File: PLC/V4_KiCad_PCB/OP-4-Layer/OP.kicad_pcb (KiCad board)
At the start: 4 copper layers, 208 x 80 mm, 307 parts, among them J1 MSTBVA-2.5-10-5.08, J10 01x03_fem, J11 01x02_fem, J12 01x15_fem, J13 01x03_fem, J14 01x15_fem, J15 01x04_fem, J16 MSTBVA-2.5-10-5.08, J17 MSTBVA-2.5-10-5.08, J2 MSTBVA-2.5-10-5.08, J25 01x05_fem, J27 Lötauge, J28 GND_CAN opt an J33, J3 PFS 2x4, J33 opt. GND_XXX, J37 Lötauge, J4 01x08_fem, J40 Extention, J41 Lötauge, J42 Lötauge, J43 Flachstecker, J44 Lötauge, J45 Lötauge, J46 Lötauge, J47 Lötauge, J48 Lötauge, J5 01x04_fem, J51 Lötauge, J52 Lötauge, J6 DIN-5, J61 Lötauge, J62 Lötauge, J7 DIN-5, J8 02x02_fem, J9 Ub 0V PE, P1 1,0K lin, P2 1,0K lin, Q1 IRLML 2244, SW1 SW_DIP_x02, SW2 SW_DIP_x02, SW3 SW_DIP_x02, U1 LTV-844, U10 ADM2483xRW, U2 LTV-844, U3 LTV-844, U36 MCP3204, U39 ADuM1401xRW, U4 LTV-844, U40 ADM-803R, U42 LM4040 AIM3-2.5, U43 LM4040 AIM3-2.5, U47 ADM-809Z, U48 ADM-803L, U49 74AHC1G32, U5 MCP23S17, U50 NE555DRG4, U6 ISO1050, U7 Teensy4.0, U8 ISO1050, U9 25LC512

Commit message: Kaltstart Überarbeitung
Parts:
- removed R50: 10k, Resistors_SMD:R_1206
- removed U40: ADM-803R, TO_SOT_Packages_SMD:SOT-23
- added C99: 100n, Capacitors_SMD:C_1206, F.Cu at (243.6, 76.6)
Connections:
- net /5V_CPU renamed Net-(C50-Pad1)
- net /COLDSTART_3V3INT renamed /3V3EN_Q2_UP
- C24 pad 2: /3V3_INTERFACE -> /3V3_INT
- C4 pad 1: /3V3_INTERFACE -> /3V3_INT
- C7 pad 2: /3V3_INTERFACE -> /3V3_INT
- C8 pad 1: /3V3_INTERFACE -> /3V3_INT
- D41 pad 2: /3V3_INTERFACE -> /3V3_INT
- J25 pad 1: /3V3_INTERFACE -> /3V3_INT
- J51 pad 1: /3V3_INTERFACE -> /3V3_INT
- R118 pad 2: /3V3_INTERFACE -> /3V3_INT
- U10 pad 1: /3V3_INTERFACE -> /3V3_INT
- U39 pad 1: /3V3_INTERFACE -> /3V3_INT
- U47 pad 3: /3V3_INTERFACE -> /3V3_INT
- U6 pad 1: /3V3_INTERFACE -> /3V3_INT
- U8 pad 1: /3V3_INTERFACE -> /3V3_INT
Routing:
- net /3V3_INTERFACE: track 182.9 -> 0.00 mm, vias 9 -> 0
- net /3V3_INT: track 217.4 -> 399.4 mm, vias 7 -> 16
- net GNDD: track 764.6 -> 762.6 mm, vias 162 -> 164

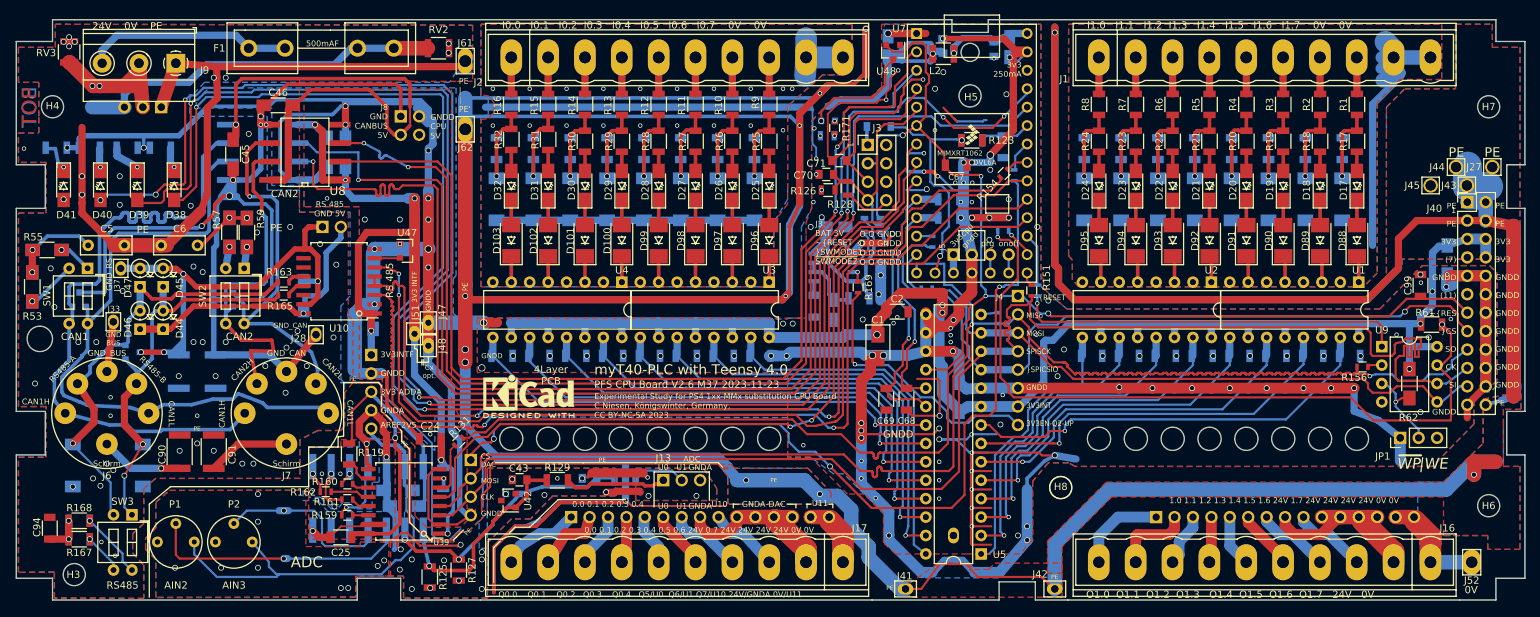
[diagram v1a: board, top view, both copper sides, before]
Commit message: Überarbeitung 4-Layer-Layout und Dokumentation
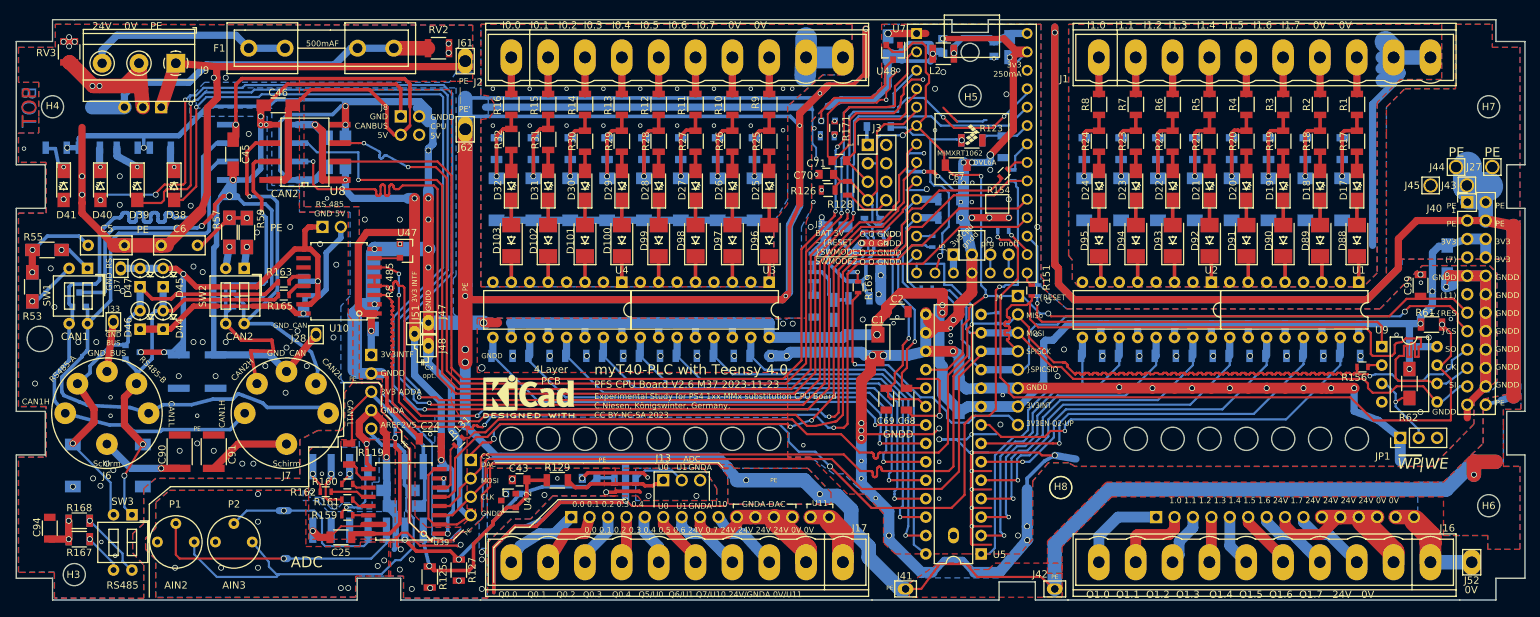
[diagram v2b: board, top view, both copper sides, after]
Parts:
- moved R155 0.13 mm to (187.5, 61.5)
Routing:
- net /3V3_INT: track 399.4 -> 421.1 mm
- net /GND_CAN_BUS: track 142.1 -> 151.8 mm
- net GNDA: track 67.8 -> 68.6 mm
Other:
- board text added: "In1"
- board text added: "In2"

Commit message: V2.6 R38 final PFS
M38 final Version for PFS variant
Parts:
- added R501: 10k, Resistors_SMD:R_1206, F.Cu at (245.4, 76.7)
- moved C99 0.51 mm to (243.1, 76.6)
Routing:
- net GNDD: track 762.6 -> 757.9 mm
- net /PE: track 1070.4 -> 1068.7 mm
- net /~EE_HOLD: vias 3 -> 2
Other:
- board text added: "PE PE 3V3 (7) (11) ~RES ~CS SO CK SI GNDD"
- board text added: "PFS CPU Board V2.6 M38 2024-01-17"
- board text removed: "PE PE 3V3 (7) GNDD (11) ~RES ~CS SO CK SI GNDD"
- board text removed: "PFS CPU Board V2.6 M37 2023-11-23"

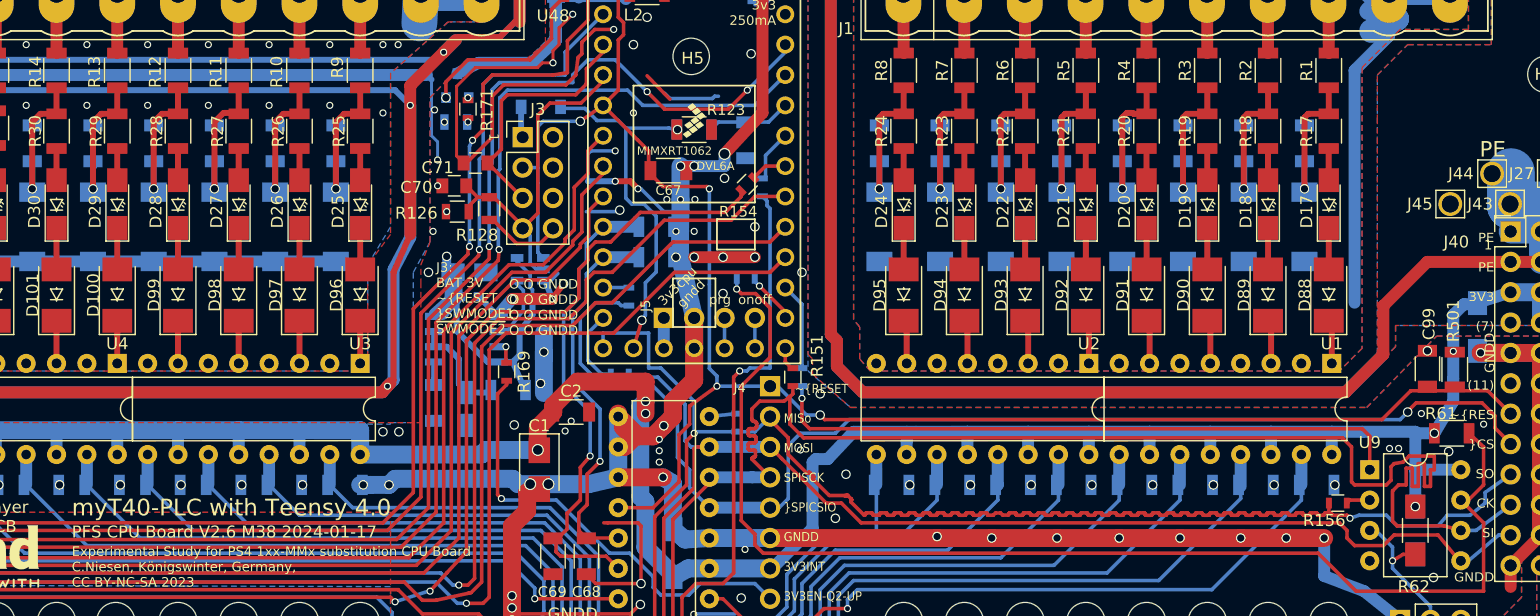
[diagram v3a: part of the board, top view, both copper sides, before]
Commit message: V2.8 M40 Coldstart Issues
Coldstart issues, some PullUps to high dimensioned, no high logic resulting together with switched-off Teensy and its input impedances.
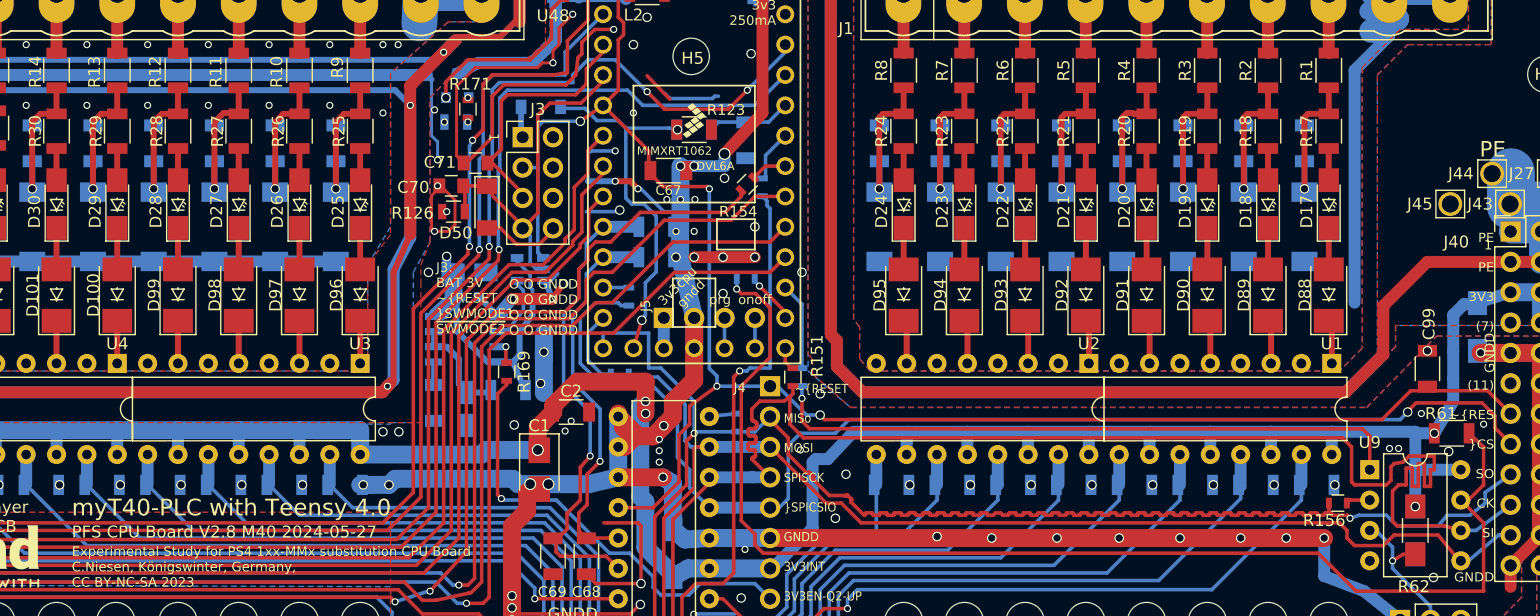
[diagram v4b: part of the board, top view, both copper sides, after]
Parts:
- removed R128: 16k, Resistors_SMD:R_0805
- removed R501: 10k, Resistors_SMD:R_1206
- added D50: 3V0, Diodes_SMD:D_MiniMELF, F.Cu at (164.4, 63.1)
- R126: value 10k -> 2k7
- moved R126 0.32 mm to (161.6, 63.5)
- moved C70 0.25 mm to (161.4, 61.3)
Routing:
- net GNDD: track 757.9 -> 768.0 mm
- net /~SW_MODE_2: track 29.1 -> 29.9 mm
- net /3V3_INT: vias 16 -> 15
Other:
- board text added: "PFS CPU Board V2.8 M40 2024-05-27"
- board text removed: "PFS CPU Board V2.6 M38 2024-01-17"
